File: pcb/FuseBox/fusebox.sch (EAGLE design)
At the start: 49 parts, among them U1 ESP32-DEVKITC-32D, U2 TEXAS_INSTRUMENTS_TPS563249DD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, U3 MAXIM_ELECTRONICS_MAX7221CWGM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, U4 NXP_PCF8574T-3,512NXP_PCF8574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

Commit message: Added some new functions to schematic and layout
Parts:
- added D1: 1N4004, diode:1N4004
- added Q1: IRF510PbF, transistor-power:PMOSFET_NTO220BV
- added X3, X5: (no value), con-wago-500:W237-102
- added X4, X6: (no value), con-wago-500:W237-103
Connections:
- new net CS_MAX7219_LEDM: U1.IO12, X4-1.KL
- new net CS_MAX7221_7SEG: U1.IO5, U3.!CS!
- new net LASER_SENSE: U1.IO26
- new net LED_RING: U1.IO27, X2-2.KL
- new net LOCK_0: Q1.G, U1.IO14
- new net N$25: D1.A, Q1.D, X5-2.KL
- new net SPI_CLK: U1.IO18, U3.CLK, X4-2.KL
- net +12V: now also D1.C, X5-1.KL
- net +3V3: now also X6-3.KL
- net +5V: now also X3-1.KL
- net GND: now also Q1.S, U1.GND1, U1.GND2, U1.GND3, X3-2.KL, X6-1.KL
- net N$23: now also X6-2.KL; no longer X2-2.KL
- net PIEZO_0: now also U1.IO13; no longer U1.SD2
- net SPI_MOSI: now also U3.DIN, X4-3.KL
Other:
- note added: "RX"
- note added: "SPI_MISO"
- note added: "TODO: LOGIK für Thomis Sensor"
- note added: "TX"
- note removed: "Pins zum MC für Ansteuerung LED Ring"

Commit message: Added second PCF8574 with some buttons and LEDs, finished I2C circuits, finished MAX7221 circuit, rearranged sheets, minor changes in circuit.
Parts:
- removed U4: NXP_PCF8574T-3,512NXP_PCF8574T-3,512_0_0, 3,512:NXP_PCF8574T-3,512NXP_PCF8574T-3,512_0_0
- added C7, C8, C9: 100n, rcl:C-EUC0805K
- added LED5, LED6, LED7, LED8: Red, led:LEDCHIP-LED0805
- added R21, R22, R23, R25, R26, R27, R28: 10k, rcl:R-EU_R0805
- added R24: 9.53k, rcl:R-EU_R0805
- added R29, R30, R31, R32: 82, rcl:R-EU_R0805
- added S10, S7, S8, S9: (no value), switch-omron:10-XX
- added U5, U6: TEXAS_INSTRUMENTS_PCF8574PWTEXAS_INSTRUMENTS_PCF8574PW_0_0, Texas Instruments - PCF8574PW:TEXAS_INSTRUMENTS_PCF8574PWTEXAS_INSTRUMENTS_PCF8574PW_0_0
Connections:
- new net BTN_DOWN: S8.P, U6.P1
- new net BTN_LEFT: S9.P, U6.P2
- new net BTN_RIGHT: S10.P, U6.P3
- new net BTN_UP: S7.P, U6.P0
- new net DIG_0: DS1.COMMON_CATHODE_D1, U3.DIG_0
- new net DIG_1: DS1.COMMON_CATHODE_D2, U3.DIG_1
- new net DIG_2: DS1.COMMON_CATHODE_D3, U3.DIG_2
- new net DIG_3: DS1.COMMON_CATHODE_D4, U3.DIG_3
- new net N$22: R23.1, U5.!INT!, U6.!INT!
- new net N$34: R28.2, S10.P1
- new net N$35: LED5.A, R29.1
- new net N$38: LED6.A, R30.1
- new net N$40: LED7.A, R31.1
- new net N$41: LED8.A, R32.1
- new net N$42: LED6.C, U6.P5
- new net N$43: LED7.C, U6.P6
- new net N$44: LED8.C, U6.P7
- net +3V3: now also C8.1, C9.1, R21.2, R22.2, R23.2, R29.2, R30.2, R31.2, R32.2, S10.S, S10.S1, S7.S, S7.S1, S8.S, S8.S1, S9.S, S9.S1, U5.VCC, U6.A0, U6.VCC; no longer U4.VDD
- net +5V: now also C7.1, R24.2
- net GND: now also C7.2, C8.2, C9.2, R25.1, R26.1, R27.1, R28.1, U5.A0, U5.A1, U5.A2, U5.GND, U6.A1, U6.A2, U6.GND; no longer U4.A0, U4.A1, U4.A2, U4.VSS
- net LASER_SENSE: now also X6-2.KL
- net N$17: now also LED5.C, U6.P4; no longer DS1.COMMON_CATHODE_D4, U3.DIG_0
- net N$18: now also R25.2, S7.P1; no longer DS1.COMMON_CATHODE_D3, U3.DIG_1
- net N$19: now also R26.2, S8.P1; no longer DS1.COMMON_CATHODE_D2, U3.DIG_2
- net N$20: now also R27.2, S9.P1; no longer DS1.COMMON_CATHODE_D1, U3.DIG_3
- net N$23: now also R24.1, U3.ISET; no longer X6-2.KL
- net N$26: now also U5.P0; no longer U4.P0
- net N$27: now also U5.P1; no longer U4.P1
- net N$28: now also U5.P2; no longer U4.P2
- net N$29: now also U5.P3; no longer U4.P3
- net N$30: now also U5.P4; no longer U4.P4
- net N$31: now also U5.P5; no longer U4.P5
- net N$32: now also U5.P6; no longer U4.P6
- net N$33: now also U5.P7; no longer U4.P7
- net SCL: now also R21.1, U5.SCL, U6.SCL; no longer U4.SCL
- net SDA: now also R22.1, U5.SDA, U6.SDA; no longer U4.SDA
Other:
- note added: "+12V Input from Power Supply"
- note added: "Connection to LED Matrix"
- note added: "Connection to Lock"
- note added: "Connection to NeoPixel ring"
- note added: "Connection to Photodiode Circuit"
- note added: "Power for LED Matrix"
- note added: "TODO: Add fuses"
- note removed: "TODO: LOGIK für Thomis Sensor"

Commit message: Some big changes
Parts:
- removed LED5, LED6, LED7, LED8: Red, led:LEDCHIP-LED0805
- removed R27, R28: 10k, rcl:R-EU_R0805
- removed R29, R30, R31, R32: 82, rcl:R-EU_R0805
- removed S10, S7, S8, S9: (no value), switch-omron:10-XX
- removed U6: TEXAS_INSTRUMENTS_PCF8574PWTEXAS_INSTRUMENTS_PCF8574PW_0_0, Texas Instruments - PCF8574PW:TEXAS_INSTRUMENTS_PCF8574PWTEXAS_INSTRUMENTS_PCF8574PW_0_0
- added TP1: TPB1,27, testpad:TPB1,27
- added U$1: NRF52840, Nordic_nRF:NRF52840
- added U4: TEXAS_INSTRUMENTS_ADS1015IDGSTTEXAS_INSTRUMENTS_ADS1015IDGS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, Texas Instruments - ADS1015IDGST:TEXAS_INSTRUMENTS_ADS1015IDGSTTEXAS_INSTRUMENTS_ADS1015IDGST_0_0
- R26: value 10k -> 237 1%; device rcl:R-EU_R0805 -> rcl:R-EU_0411/15
- S1, S2, S3, S4, S5, S6: value (none) -> MOMENTARY-SWITCH-SPST-SMD-6.2MM-TALL; device switch-omron:10-XX -> SparkFun-Switches:MOMENTARY-SWITCH-SPST-SMD-6.2MM-TALL
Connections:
- removed net BTN_DOWN: S8.P, U6.P1
- removed net BTN_LEFT: S9.P, U6.P2
- removed net BTN_RIGHT: S10.P, U6.P3
- removed net BTN_UP: S7.P, U6.P0
- removed net N$18: R25.2, S7.P1
- removed net N$19: R26.2, S8.P1
- removed net N$20: R27.2, S9.P1
- removed net N$21: R19.2, S5.P1
- removed net N$22: R23.1, U5.!INT!, U6.!INT!
- removed net N$24: R20.2, S6.P1
- removed net N$34: R28.2, S10.P1
- removed net N$35: LED5.A, R29.1
- removed net N$38: LED6.A, R30.1
- removed net N$40: LED7.A, R31.1
- removed net N$41: LED8.A, R32.1
- removed net N$42: LED6.C, U6.P5
- removed net N$43: LED7.C, U6.P6
- removed net N$44: LED8.C, U6.P7
- new net ADC_RDY: R25.1, U1.IO4, U4.ALERT/RDY
- new net PCF_INT: R23.1, U1.IO15, U5.!INT!
- net +12V: now also TP1.TP
- net +3V3: now also R25.2, S5.2, S6.2, U4.VDD; no longer R29.2, R30.2, R31.2, R32.2, S10.S, S10.S1, S5.S, S5.S1, S6.S, S6.S1, S7.S, S7.S1, S8.S, S8.S1, S9.S, S9.S1, U6.A0, U6.VCC
- net BUTTON_0: now also R19.2, S5.1; no longer S5.P
- net BUTTON_1: now also R20.2, S6.1; no longer S6.P
- net GND: now also S1.2, S2.2, S3.2, S4.2, U4.ADDR, U4.GND; no longer R25.1, R26.1, R27.1, R28.1, S1.S, S1.S1, S2.S, S2.S1, S3.S, S3.S1, S4.S, S4.S1, U6.A1, U6.A2, U6.GND
- net N$11: now also S4.1; no longer S4.P, S4.P1
- net N$17: now also R26.1, R26.2; no longer LED5.C, U6.P4
- net N$5: now also S1.1; no longer S1.P, S1.P1
- net N$7: now also S2.1; no longer S2.P, S2.P1
- net N$9: now also S3.1; no longer S3.P, S3.P1
- net POTI_0: now also U4.AIN0; no longer U1.IO15
- net POTI_1: now also U4.AIN1; no longer U1.IO2
- net POTI_2: now also U4.AIN2; no longer U1.IO0
- net POTI_3: now also U4.AIN3; no longer U1.IO4
- net SCL: now also U4.SCL; no longer U6.SCL
- net SDA: now also U4.SDA; no longer U6.SDA
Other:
- note added: "Do not use IO2 and IO0, those are selecting bootmode and should be left unconnected/floating"
- note added: "Do not use SDO, SD1, SD2, SD3, CLK and CMD, they're connected to integrated SPI Flash"
- moved on the sheet: C8, C9, JP3, JP4, LED1, LED2, LED3, LED4, LS1, R1, R19, R2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

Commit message: Further work on PCB
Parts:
- removed U$1: NRF52840, Nordic_nRF:NRF52840
- added C10: 100n, rcl:C-EUC0805K
- added F1: MF-SMDF150, fuse:MF-SMDF150
- added LED5, LED6, LED7, LED8: Red, led:LEDCHIP-LED0805
- added R27, R32, R33, R34, R35: 10k, rcl:R-EU_R0805
- added R28, R29, R30, R31: 82, rcl:R-EU_R0805
- added S10, S7, S8, S9: MOMENTARY-SWITCH-SPST-SMD-6.2MM-TALL, SparkFun-Switches:MOMENTARY-SWITCH-SPST-SMD-6.2MM-TALL
- added TP10, TP11, TP12, TP13, TP14, TP15, TP16, TP17, TP2, TP3, TP4, TP5, TP6, TP7, TP8, TP9: TPB1,27, testpad:TPB1,27
- added U6: TEXAS_INSTRUMENTS_PCF8574PWTEXAS_INSTRUMENTS_PCF8574PW_0_0, Texas Instruments - PCF8574PW:TEXAS_INSTRUMENTS_PCF8574PWTEXAS_INSTRUMENTS_PCF8574PW_0_0
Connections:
- net N$10 renamed SEG_C
- net N$12 renamed SEG_D
- net N$13 renamed SEG_DP
- net N$14 renamed SEG_E
- net N$15 renamed SEG_F
- net N$16 renamed SEG_G
- net N$6 renamed SEG_A
- net N$8 renamed SEG_B
- removed net PCF_INT: R23.1, U1.IO15, U5.!INT!
- new net N$18: C1.1, C2.1, C3.1, F1.2, TP1.TP, U2.EN, U2.VIN
- new net N$19: LED5.C, U6.P0
- new net N$20: LED6.A, R29.1
- new net N$21: LED6.C, U6.P1
- new net N$22: LED7.A, R30.1
- new net N$24: LED7.C, U6.P2
- new net N$34: LED8.A, R31.1
- new net N$35: LED8.C, U6.P3
- new net P4_BTN7: R32.2, S7.1, U6.P4
- new net P5_BTN8: R33.2, S8.1, U6.P5
- new net P6_BTN9: R34.2, S9.1, U6.P6
- new net P7_BTN10: R35.2, S10.1, U6.P7
- new net PCF_INT_0: R23.1, TP16.TP, U1.SENSOR_VN, U5.!INT!
- new net PCF_INT_1: R27.1, TP15.TP, U1.SENSOR_VP, U6.!INT!
- net +0V9: now also TP5.TP
- net +12V: now also F1.1; no longer C1.1, C2.1, C3.1, TP1.TP, U2.EN, U2.VIN
- net +1V5: now also TP4.TP
- net +2V1: now also TP3.TP
- net +2V7: now also TP2.TP
- net +3V3: now also C10.1, R27.2, R28.2, R29.2, R30.2, R31.2, S10.2, S7.2, S8.2, S9.2, U6.A0, U6.VCC
- net +5V: now also TP6.TP
- net ADC_RDY: now also TP14.TP
- net CS_MAX7219_LEDM: now also TP17.TP
- net CS_MAX7221_7SEG: now also TP13.TP
- net GND: now also C10.2, R26.1, R26.2, R32.1, R33.1, R34.1, R35.1, TP7.TP, U6.A1, U6.A2, U6.GND
- net N$17: now also LED5.A, R28.1; no longer R26.1, R26.2
- net N$39: now also TP8.TP
- net SCL: now also TP10.TP, U6.SCL
- net SDA: now also TP11.TP, U6.SDA
- net SPI_CLK: now also TP9.TP
- net SPI_MOSI: now also TP12.TP
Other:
- note removed: "TODO: Add fuses"
- moved on the sheet: C8, C9, JP3, JP4, R21, R22, R23, R25, U4, U5

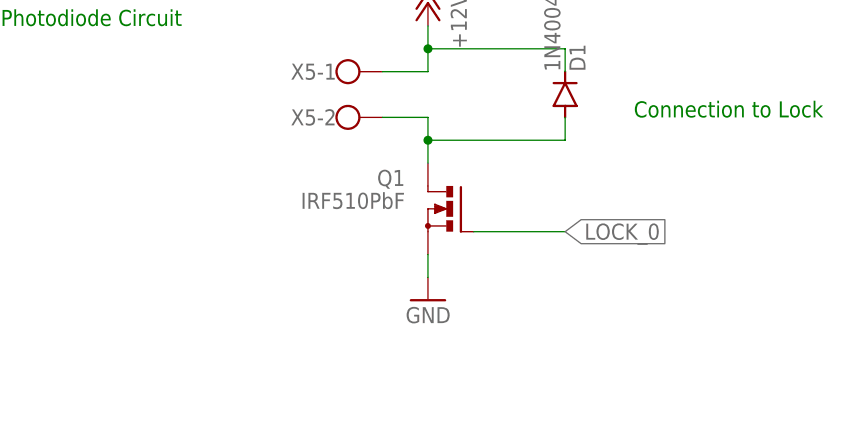
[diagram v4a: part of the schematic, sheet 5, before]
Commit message: Further work on PCB, almost done. Just have to route I2C and SPI lanes.
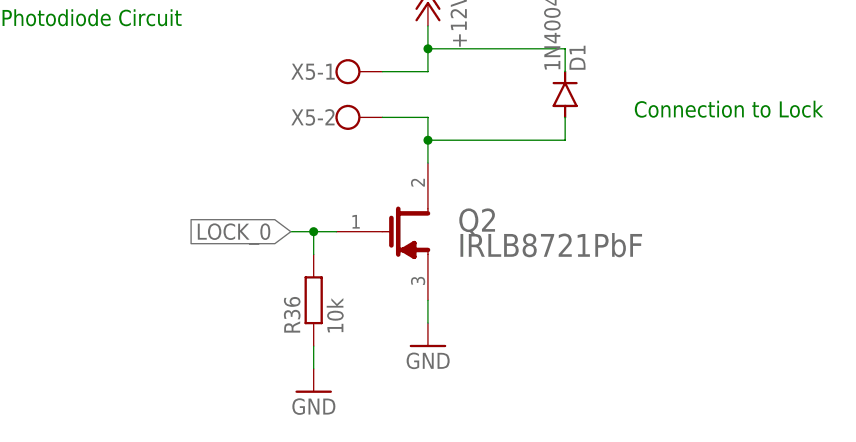
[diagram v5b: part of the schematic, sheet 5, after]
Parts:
- removed Q1: IRF510PbF, transistor-power:PMOSFET_NTO220BV
- added Q2: INFINEON_IRLB8721PBFINFINEON_IRLB8721PBF_0_0, Infineon - IRLB8721PbF:INFINEON_IRLB8721PBFINFINEON_IRLB8721PBF_0_0
- added R36: 10k, rcl:R-EU_R0805
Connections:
- net GND: now also Q2.S, R36.1; no longer Q1.S
- net LOCK_0: now also Q2.G, R36.2; no longer Q1.G
- net N$25: now also Q2.D; no longer Q1.D
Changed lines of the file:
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@@
 <part name="X3" library="con-wago-500" library_urn="urn:adsk.eagle:library:195" deviceset="W237-102" device="" package3d_urn="urn:adsk.eagle:package:10688/1"/>
 <part name="X4" library="con-wago-500" library_urn="urn:adsk.eagle:library:195" deviceset="W237-103" device="" package3d_urn="urn:adsk.eagle:package:10691/1"/>
-<part name="Q1" library="transistor-power" library_urn="urn:adsk.eagle:library:400" deviceset="PMOSFET_N" device="TO220BV" package3d_urn="urn:adsk.eagle:package:29484/3" value="IRF510PbF"/>
 <part name="X5" library="con-wago-500" library_urn="urn:adsk.eagle:library:195" deviceset="W237-102" device="" package3d_urn="urn:adsk.eagle:package:10688/1"/>
 <part name="P+8" library="supply1" library_urn="urn:adsk.eagle:library:371" deviceset="+12V" device=""/>
@@
 <part name="TP16" library="testpad" library_urn="urn:adsk.eagle:library:385" deviceset="TP" device="B1,27" package3d_urn="urn:adsk.eagle:package:27944/2"/>
 <part name="TP17" library="testpad" library_urn="urn:adsk.eagle:library:385" deviceset="TP" device="B1,27" package3d_urn="urn:adsk.eagle:package:27944/2"/>
+<part name="Q2" library="Infineon - IRLB8721PbF" deviceset="INFINEON_IRLB8721PBF" device="INFINEON_IRLB8721PBF_0_0" package3d_urn="urn:adsk.eagle:package:15923357/1"/>
+<part name="R36" library="rcl" library_urn="urn:adsk.eagle:library:334" deviceset="R-EU_" device="R0805" package3d_urn="urn:adsk.eagle:package:23553/2" value="10k"/>
+<part name="GND37" library="supply1" library_urn="urn:adsk.eagle:library:371" deviceset="GND" device=""/>
 </parts>
 <sheets>
@@
 <attribute name="NAME" x="114.3" y="150.749" size="1.778" layer="95" rot="R180"/>
 </instance>
-<instance part="Q1" gate="G$1" x="200.66" y="111.76" smashed="yes" rot="MR0">
-<attribute name="NAME" x="195.58" y="114.3" size="1.778" layer="95" rot="MR0"/>
-<attribute name="VALUE" x="195.58" y="111.76" size="1.778" layer="96" rot="MR0"/>
-</instance>
 <instance part="X5" gate="-1" x="187.96" y="127" smashed="yes">
 <attribute name="NAME" x="187.96" y="127.889" size="1.778" layer="95" rot="R180"/>
@@
 <attribute name="VALUE" x="211.0486" y="127" size="1.778" layer="96" rot="MR90"/>
 </instance>
-<instance part="GND21" gate="1" x="198.12" y="101.6" smashed="yes" rot="MR0">
-<attribute name="VALUE" x="200.66" y="99.06" size="1.778" layer="96" rot="MR0"/>
+<instance part="GND21" gate="1" x="198.12" y="96.52" smashed="yes" rot="MR0">
+<attribute name="VALUE" x="200.66" y="93.98" size="1.778" layer="96" rot="MR0"/>
 </instance>
 <instance part="X6" gate="-1" x="114.3" y="121.92" smashed="yes" rot="MR180">
@@
 <instance part="GND14" gate="1" x="55.88" y="101.6" smashed="yes">
 <attribute name="VALUE" x="53.34" y="99.06" size="1.778" layer="96"/>
+</instance>
+<instance part="Q2" gate="G$0" x="193.04" y="114.3" smashed="yes">
+<attribute name="NAME" x="201.422" y="111.76" size="2.54" layer="95" align="top-left"/>
+</instance>
+<instance part="R36" gate="G$1" x="185.42" y="101.6" smashed="yes" rot="R90">
+<attribute name="NAME" x="183.9214" y="97.79" size="1.778" layer="95" rot="R90"/>
+<attribute name="VALUE" x="188.722" y="97.79" size="1.778" layer="96" rot="R90"/>
+</instance>
+<instance part="GND37" gate="1" x="185.42" y="91.44" smashed="yes" rot="MR0">
+<attribute name="VALUE" x="187.96" y="88.9" size="1.778" layer="96" rot="MR0"/>
 </instance>
 </instances>
@@
 </segment>
 <segment>
-<pinref part="Q1" gate="G$1" pin="S"/>
-<wire x1="198.12" y1="106.68" x2="198.12" y2="104.14" width="0.1524" layer="91"/>
-<pinref part="GND21" gate="1" pin="GND"/>
-</segment>
-<segment>
 <pinref part="GND22" gate="1" pin="GND"/>
 <wire x1="124.46" y1="116.84" x2="124.46" y2="121.92" width="0.1524" layer="91"/>
@@
 <wire x1="55.88" y1="109.22" x2="50.8" y2="109.22" width="0.1524" layer="91"/>
 </segment>
+<segment>
+<pinref part="GND21" gate="1" pin="GND"/>
+<pinref part="Q2" gate="G$0" pin="S"/>
+<wire x1="198.12" y1="99.06" x2="198.12" y2="101.6" width="0.1524" layer="91"/>
+</segment>
+<segment>
+<pinref part="GND37" gate="1" pin="GND"/>
+<pinref part="R36" gate="G$1" pin="1"/>
+<wire x1="185.42" y1="93.98" x2="185.42" y2="96.52" width="0.1524" layer="91"/>
+</segment>
 </net>
 <net name="SPI_MOSI" class="0">
@@
 <net name="LOCK_0" class="0">
 <segment>
-<pinref part="Q1" gate="G$1" pin="G"/>
-<wire x1="203.2" y1="109.22" x2="213.36" y2="109.22" width="0.1524" layer="91"/>
-<label x="213.36" y="109.22" size="1.778" layer="95" rot="MR180" xref="yes"/>
+<wire x1="187.96" y1="109.22" x2="185.42" y2="109.22" width="0.1524" layer="91"/>
+<label x="182.88" y="109.22" size="1.778" layer="95" rot="MR0" xref="yes"/>
+<pinref part="Q2" gate="G$0" pin="G"/>
+<pinref part="R36" gate="G$1" pin="2"/>
+<wire x1="185.42" y1="109.22" x2="182.88" y2="109.22" width="0.1524" layer="91"/>
+<wire x1="185.42" y1="106.68" x2="185.42" y2="109.22" width="0.1524" layer="91"/>
+<junction x="185.42" y="109.22"/>
 </segment>
 </net>
@@
 <net name="N$25" class="0">
 <segment>
-<pinref part="Q1" gate="G$1" pin="D"/>
 <wire x1="198.12" y1="116.84" x2="198.12" y2="119.38" width="0.1524" layer="91"/>
 <pinref part="X5" gate="-2" pin="KL"/>
@@
 <wire x1="213.36" y1="119.38" x2="198.12" y2="119.38" width="0.1524" layer="91"/>
 <junction x="198.12" y="119.38"/>
-</segment>
-</net>
+<pinref part="Q2" gate="G$0" pin="D"/>
+</segment>
+</net>
